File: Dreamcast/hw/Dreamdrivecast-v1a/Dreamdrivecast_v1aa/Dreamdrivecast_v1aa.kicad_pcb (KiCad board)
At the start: 4 copper layers, 96 x 94.2 mm, 69 parts, among them J1 USB_C_Receptacle_USB2.0, J2 Micro_SD_Card, J4 Dreamcast Data, J5 USB_C_Receptacle_USB2.0, J6 Dreamcast Control Lines, J7 MCU Databus, J9 MCU Misc, U1 W25Q128JVS, U2 AMS1117-3.3, U3 SRV05-4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

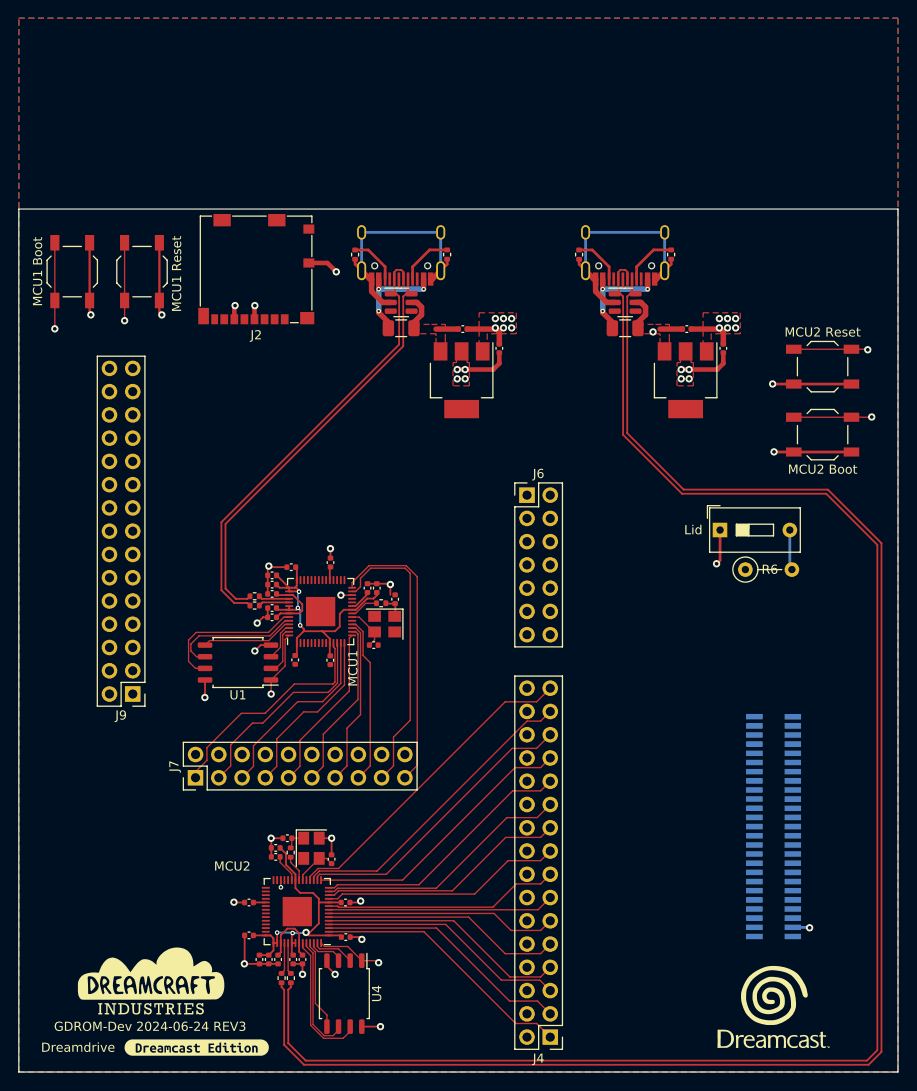
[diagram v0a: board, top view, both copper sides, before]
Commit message: Routed another version of the board that includes a bunch of breakout headers. The routing is messing and it needs to have a single power net.
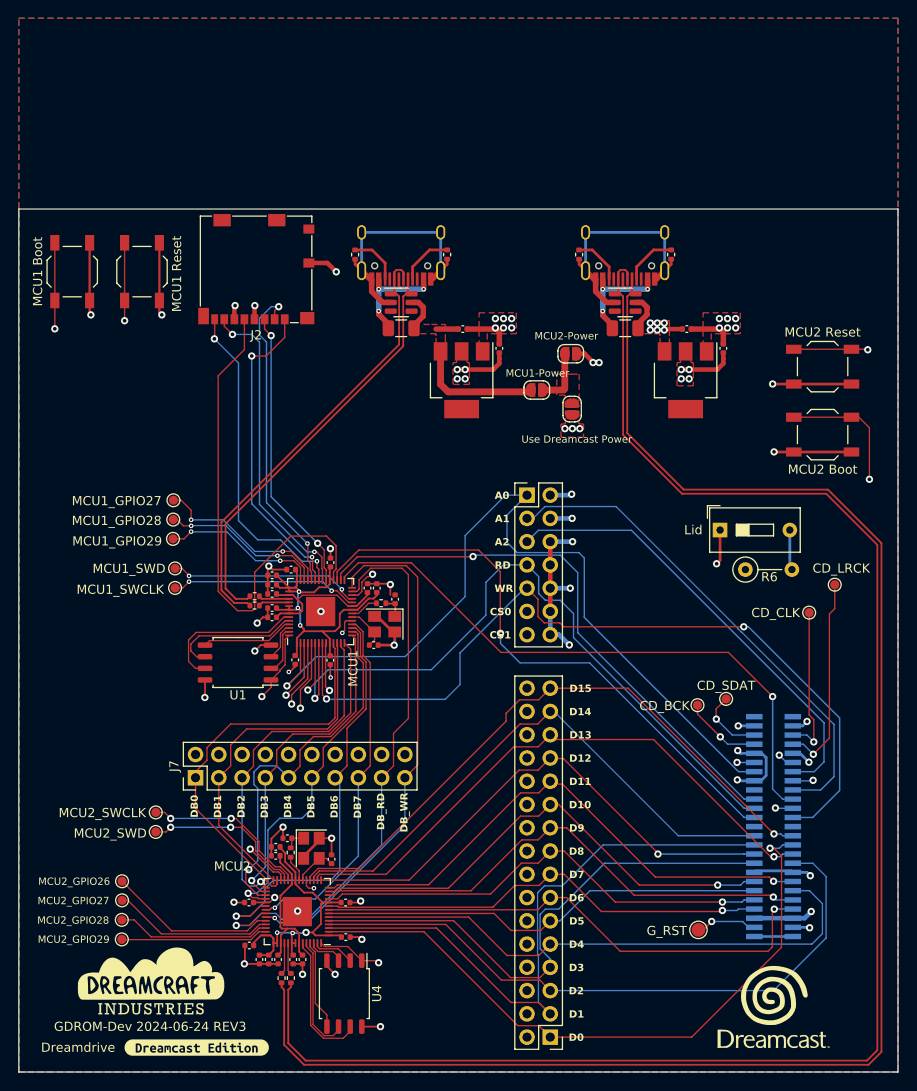
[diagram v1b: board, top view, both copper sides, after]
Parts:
- removed J9: MCU Misc, Connector_PinHeader_2.54mm:PinHeader_2x15_P2.54mm_Vertical
- added CD_BCK: TestPoint_Pad_D1.0mm, TestPoint:TestPoint_Pad_D1.0mm, F.Cu at (133.7, 123.8)
- added CD_CLK: TestPoint_Pad_D1.0mm, TestPoint:TestPoint_Pad_D1.0mm, F.Cu at (145.9, 113.7)
- added CD_LRCK: TestPoint_Pad_D1.0mm, TestPoint:TestPoint_Pad_D1.0mm, F.Cu at (148.7, 110.6)
- added CD_SDAT: TestPoint_Pad_D1.0mm, TestPoint:TestPoint_Pad_D1.0mm, F.Cu at (136.8, 123.1)
- added G_RST: TestPoint_Pad_D1.5mm, TestPoint:TestPoint_Pad_D1.5mm, F.Cu at (133.8, 148.3)
- added MCU1-Power: SolderJumper-2_P1.3mm_Open_RoundedPad1.0x1.5mm, Jumper:SolderJumper-2_P1.3mm_Open_RoundedPad1.0x1.5mm, F.Cu at (116.1, 89.4)
- added MCU1_GPIO27: TestPoint_Pad_D1.0mm, TestPoint:TestPoint_Pad_D1.0mm, F.Cu at (76.5, 101.4)
- added MCU1_GPIO28: TestPoint_Pad_D1.0mm, TestPoint:TestPoint_Pad_D1.0mm, F.Cu at (76.4, 103.5)
- added MCU1_GPIO29: TestPoint_Pad_D1.0mm, TestPoint:TestPoint_Pad_D1.0mm, F.Cu at (76.4, 105.6)
- added MCU1_SWCLK: TestPoint_Pad_D1.0mm, TestPoint:TestPoint_Pad_D1.0mm, F.Cu at (76.6, 111.0)
- added MCU1_SWD: TestPoint_Pad_D1.0mm, TestPoint:TestPoint_Pad_D1.0mm, F.Cu at (76.6, 108.8)
- added MCU2-Power: SolderJumper-2_P1.3mm_Open_RoundedPad1.0x1.5mm, Jumper:SolderJumper-2_P1.3mm_Open_RoundedPad1.0x1.5mm, F.Cu at (119.8, 85.4)
- added MCU2_GPIO26: TestPoint_Pad_D1.0mm, TestPoint:TestPoint_Pad_D1.0mm, F.Cu at (70.8, 143.0)
- added MCU2_GPIO27: TestPoint_Pad_D1.0mm, TestPoint:TestPoint_Pad_D1.0mm, F.Cu at (70.8, 145.1)
- added MCU2_GPIO28: TestPoint_Pad_D1.0mm, TestPoint:TestPoint_Pad_D1.0mm, F.Cu at (70.8, 147.2)
- added MCU2_GPIO29: TestPoint_Pad_D1.0mm, TestPoint:TestPoint_Pad_D1.0mm, F.Cu at (70.8, 149.4)
- added MCU2_SWCLK: TestPoint_Pad_D1.0mm, TestPoint:TestPoint_Pad_D1.0mm, F.Cu at (74.5, 135.5)
- added MCU2_SWD: TestPoint_Pad_D1.0mm, TestPoint:TestPoint_Pad_D1.0mm, F.Cu at (74.5, 137.6)
- added Use Dreamcast Power: SolderJumper-2_P1.3mm_Open_RoundedPad1.0x1.5mm, Jumper:SolderJumper-2_P1.3mm_Open_RoundedPad1.0x1.5mm, F.Cu at (120.0, 91.4)
- moved C24 1.10 mm to (84.7, 150.0)
- moved C9 0.26 mm to (89.3, 109.0)
- moved C17 0.12 mm to (87.6, 140.2)
- moved C25 0.12 mm to (87.6, 139.2)
- renumbered REF** to C14
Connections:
- R6 pad 1: +5V -> 5V
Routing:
- net /A1: track 0.00 -> 96.8 mm, vias 0 -> 1
- net /A2: track 0.00 -> 92.0 mm, vias 0 -> 1
- net /A0: track 0.00 -> 91.3 mm, vias 0 -> 1
- net /WR: track 0.00 -> 90.4 mm, vias 0 -> 2
- net Dreamcast_5V: track 0.00 -> 80.3 mm, vias 0 -> 4
- net /RD: track 0.00 -> 77.0 mm, vias 0 -> 1
- net /IORDY: track 0.00 -> 69.3 mm, vias 0 -> 2
- net 5V: track 12.8 -> 81.7 mm, vias 0 -> 8
- net /INTRQ: track 0.00 -> 66.6 mm, vias 0 -> 1
- net /CS1: track 0.00 -> 66.6 mm, vias 0 -> 2
- net /DMARQ: track 0.00 -> 64.1 mm, vias 0 -> 1
- net /CS0: track 0.00 -> 63.5 mm, vias 0 -> 2
- net GND: track 141.2 -> 202.8 mm, vias 32 -> 51
- net /DMACK: track 0.00 -> 61.6 mm, vias 0 -> 1
- net /SD_CLK: track 0.00 -> 54.6 mm
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- added copper zone on F.Cu, net Dreamcast_5V
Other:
- board text added: "A0"
- board text added: "A1"
- board text added: "A2"
- board text added: "CS0"
- board text added: "CS1"
- board text added: "D0"
- board text added: "D1"
- board text added: "D10"
- board text added: "D11"
- board text added: "D12"
- board text added: "D13"
- board text added: "D14"
- board text added: "D15"
- board text added: "D2"
- board text added: "D3"
- board text added: "D4"
- board text added: "D5"
- board text added: "D6"
- board text added: "D7"
- board text added: "D8"
- board text added: "D9"
- board text added: "DB0"
- board text added: "DB1"
- board text added: "DB2"
- board text added: "DB3"
- board text added: "DB4"
- board text added: "DB5"
- board text added: "DB6"
- board text added: "DB7"
- board text added: "DB_RD"
- board text added: "DB_WR"
- board text added: "RD"
- board text added: "WR"

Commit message: Update pcb and schematic to reflect diode and removal of second mosfet connected to mcu2
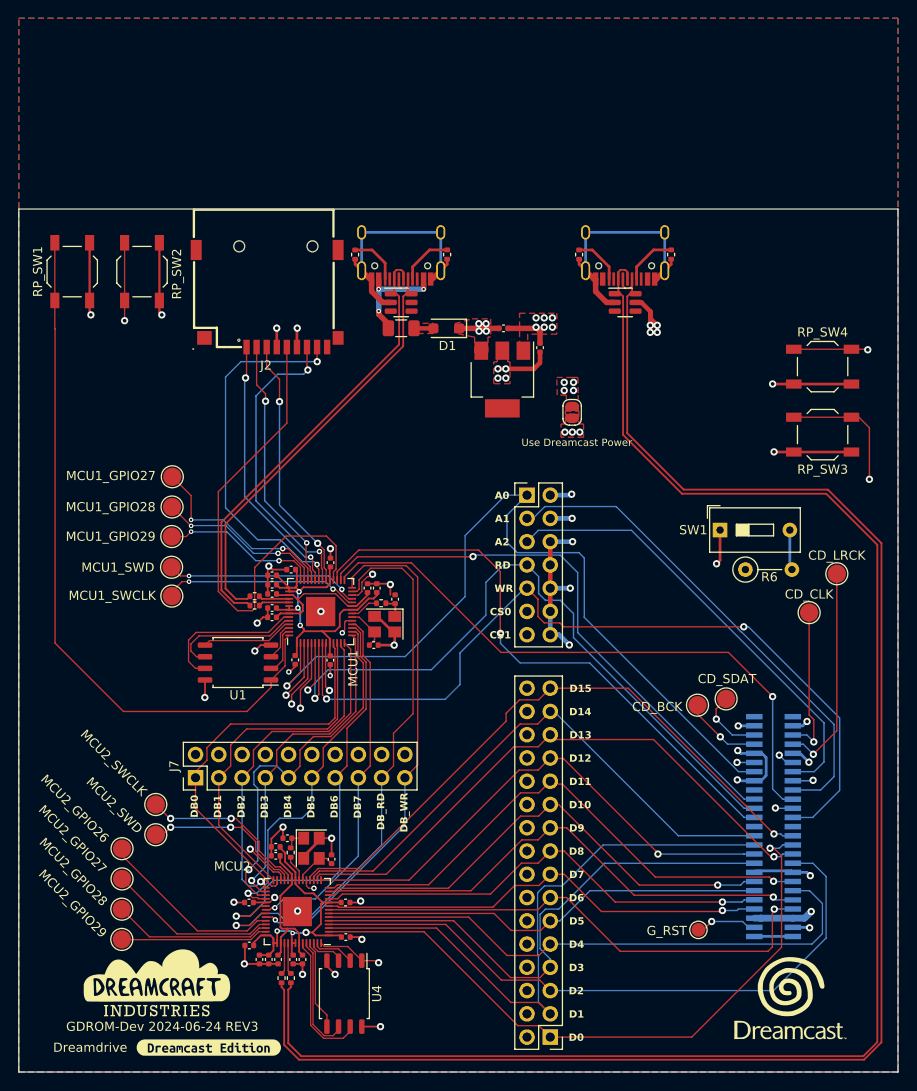
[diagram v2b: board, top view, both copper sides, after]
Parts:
- removed C29, C30: 1uF, Capacitor_SMD:C_0402_1005Metric
- removed F2: 1.1A, Fuse:Fuse_1206_3216Metric
- removed MCU1-Power, MCU2-Power: SolderJumper-2_P1.3mm_Open_RoundedPad1.0x1.5mm, Jumper:SolderJumper-2_P1.3mm_Open_RoundedPad1.0x1.5mm
- removed U5: AMS1117-3.3, Package_TO_SOT_SMD:SOT-223
- added D1: D_Schottky, Diode_SMD:D_SOD-123F, F.Cu at (106.2, 82.6)
- CD_BCK, CD_CLK, CD_LRCK, CD_SDAT, MCU1_GPIO27, MCU1_GPIO28, MCU1_GPIO29, MCU1_SWCLK, MCU1_SWD, MCU2_GPIO26, MCU2_GPIO27, MCU2_GPIO28, MCU2_GPIO29, MCU2_SWCLK, MCU2_SWD: value TestPoint_Pad_D1.0mm -> TestPoint_Pad_D2.0mm; footprint TestPoint:TestPoint_Pad_D1.0mm -> TestPoint:TestPoint_Pad_D2.0mm
- J2: footprint Connector_Card:microSD_HC_Molex_104031-0811 -> sd_card_lib:TF-SMD_TF-PUSH
- RP_SW1: renamed from MCU1 Boot
- RP_SW2: renamed from MCU1 Reset
- RP_SW3: renamed from MCU2 Boot
- RP_SW4: renamed from MCU2 Reset
- moved C14 4.45 mm to (112.5, 82.6)
- moved U2 4.45 mm to (112.4, 88.2)
- moved C15 4.45 mm to (116.5, 84.7)
- moved MCU2_GPIO26 3.56 mm to (70.8, 139.4)
- moved J2 3.40 mm to (86.7, 79.4)
- moved MCU1_GPIO27 2.57 mm to (76.3, 98.8)
- moved MCU2_GPIO27 2.34 mm to (70.8, 142.7)
- moved G*** 2.07 mm to (143.8, 155.8)
- moved MCU1_GPIO28 1.38 mm to (76.3, 102.1)
- moved kibuzzard-63F149CE 1.32 mm to (80.3, 161.2)
- moved CD_LRCK 1.22 mm to (148.9, 109.4)
- moved MCU2_GPIO28 1.17 mm to (70.8, 146.1)
- moved MCU1_SWCLK 0.96 mm to (76.3, 111.9)
- moved MCU2_SWCLK 0.86 mm to (74.5, 134.6)
- moved DREAMCRAFT_LOGO 0.67 mm to (74.6, 154.5)
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- renumbered Dreamcast to CN1, Lid to SW1
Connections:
- F1 pad 1: 5V -> VBUS
- F1 pad 2: Net-(F1-Pad2) -> VBUS
- J1 pad A4: Net-(F1-Pad2) -> VBUS
- J1 pad A9: Net-(F1-Pad2) -> VBUS
- J1 pad B4: Net-(F1-Pad2) -> VBUS
- J1 pad B9: Net-(F1-Pad2) -> VBUS
- J5 pad A4: Net-(F1-Pad2) -> VBUS
- J5 pad A9: Net-(F1-Pad2) -> VBUS
- J5 pad B4: Net-(F1-Pad2) -> VBUS
- J5 pad B9: Net-(F1-Pad2) -> VBUS
- R6 pad 1: 5V -> +5V
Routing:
- net 5V: track 81.7 -> 10.8 mm, vias 8 -> 12
- net Net-(F1-Pad2): track 22.8 -> 0.00 mm, vias 6 -> 0
- net VBUS: track 0.00 -> 13.2 mm, vias 0 -> 3
- net GND: track 202.8 -> 194.7 mm, vias 51 -> 44
- net /SD_DAT3: track 35.1 -> 28.1 mm
- net RP1_CS: track 84.3 -> 78.0 mm, vias 2 -> 0
- net 3.3V: track 91.6 -> 85.8 mm, vias 18 -> 14
- net /SD_DAT1: track 35.6 -> 40.9 mm
- net /SD_DAT2: track 34.2 -> 29.1 mm
- net /SD_CMD: track 31.3 -> 28.1 mm
- net /MCU1_GPIO27: track 19.7 -> 21.8 mm
- net /MCU2_GPIO26: track 18.4 -> 20.3 mm
- net RP1_RUN_PULL: track 52.7 -> 51.2 mm
- net /SD_DAT0: track 34.8 -> 33.4 mm
- net Dreamcast_5V: track 80.3 -> 79.0 mm
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- added copper zone on In1.Cu, net 5V
- added copper zone on In1.Cu, net Dreamcast_5V
- added copper zone on F.Cu, net VBUS

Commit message: MIXED COMMIT: Dreamcast related: Data looks like it's flowing correctly! Dreamdrive: Modifed ctr0.s file has been included so others can drop into their pico-sdk folder. Dumper files have been updated with new design.
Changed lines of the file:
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@@
     )
     (fp_line (start -7.259995 -3.249936) (end -7.259995 3.910084)
-      (stroke (width 0.254001) (type solid)) (layer "F.SilkS"))
+      (stroke (width 0.254) (type solid)) (layer "F.SilkS"))
     (fp_line (start -7.239954 9.700051) (end -7.239954 6.76002)
-      (stroke (width 0.254001) (type solid)) (layer "F.SilkS"))
+      (stroke (width 0.254) (type solid)) (layer "F.SilkS"))
     (fp_line (start -7.239954 9.700051) (end 8 9.700051)
-      (stroke (width 0.254001) (type solid)) (layer "F.SilkS"))
+      (stroke (width 0.254) (type solid)) (layer "F.SilkS"))
     (fp_line (start 4.702057 -5.299721) (end 5.489459 -5.299721)
-      (stroke (width 0.254001) (type solid)) (layer "F.SilkS"))
+      (stroke (width 0.254) (type solid)) (layer "F.SilkS"))
     (fp_line (start 4.702159 -5.299975) (end 2.849987 -5.299975)
-      (stroke (width 0.254001) (type solid)) (layer "F.SilkS"))
+      (stroke (width 0.254) (type solid)) (layer "F.SilkS"))
     (fp_line (start 5.489459 -5.299721) (end 5.489459 -3.199136)
-      (stroke (width 0.254001) (type solid)) (layer "F.SilkS"))
+      (stroke (width 0.254) (type solid)) (layer "F.SilkS"))
     (fp_line (start 5.489459 -3.199136) (end 5.500025 -3.199975)
-      (stroke (width 0.254001) (type solid)) (layer "F.SilkS"))
+      (stroke (width 0.254) (type solid)) (layer "F.SilkS"))
     (fp_line (start 7.980036 -3.199949) (end 5.490018 -3.199975)
-      (stroke (width 0.254001) (type solid)) (layer "F.SilkS"))
+      (stroke (width 0.254) (type solid)) (layer "F.SilkS"))
     (fp_line (start 7.980036 3.96886) (end 7.980036 -3.199949)
-      (stroke (width 0.254001) (type solid)) (layer "F.SilkS"))
+      (stroke (width 0.254) (type solid)) (layer "F.SilkS"))
     (fp_line (start 8 9.700051) (end 8 6.710033)
-      (stroke (width 0.254001) (type solid)) (layer "F.SilkS"))
+      (stroke (width 0.254) (type solid)) (layer "F.SilkS"))
     (fp_circle (center 3.087122 -4.551943) (end 3.139446 -4.551943)
-      (stroke (width 0.254001) (type solid)) (fill none) (layer "F.SilkS"))
+      (stroke (width 0.254) (type solid)) (fill none) (layer "F.SilkS"))
     (fp_circle (center 8.069977 -5.505207) (end 8.099975 -5.505207)
       (stroke (width 0.059995) (type solid)) (fill none) (layer "F.SilkS"))
@@
       (stroke (width 0.4) (type solid)) (fill none) (layer "F.Fab"))
     (fp_circle (center 2.810008 -5.629997) (end 2.937008 -5.629997)
-      (stroke (width 0.254001) (type solid)) (fill none) (layer "F.Fab"))
+      (stroke (width 0.254) (type solid)) (fill none) (layer "F.Fab"))
     (fp_circle (center 3.050038 5.700025) (end 3.250038 5.700025)
       (stroke (width 0.4) (type solid)) (fill none) (layer "F.Fab"))
